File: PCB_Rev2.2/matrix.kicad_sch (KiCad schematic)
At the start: 9 parts, among them SW10 SW_Push, SW2 RotaryEncoder_Switch_MP, SW3 RotaryEncoder_Switch_MP, SW4 SW_Push, SW5 SW_Push, SW6 SW_Push, SW7 SW_Push, SW8 SW_Push, SW9 SW_Push

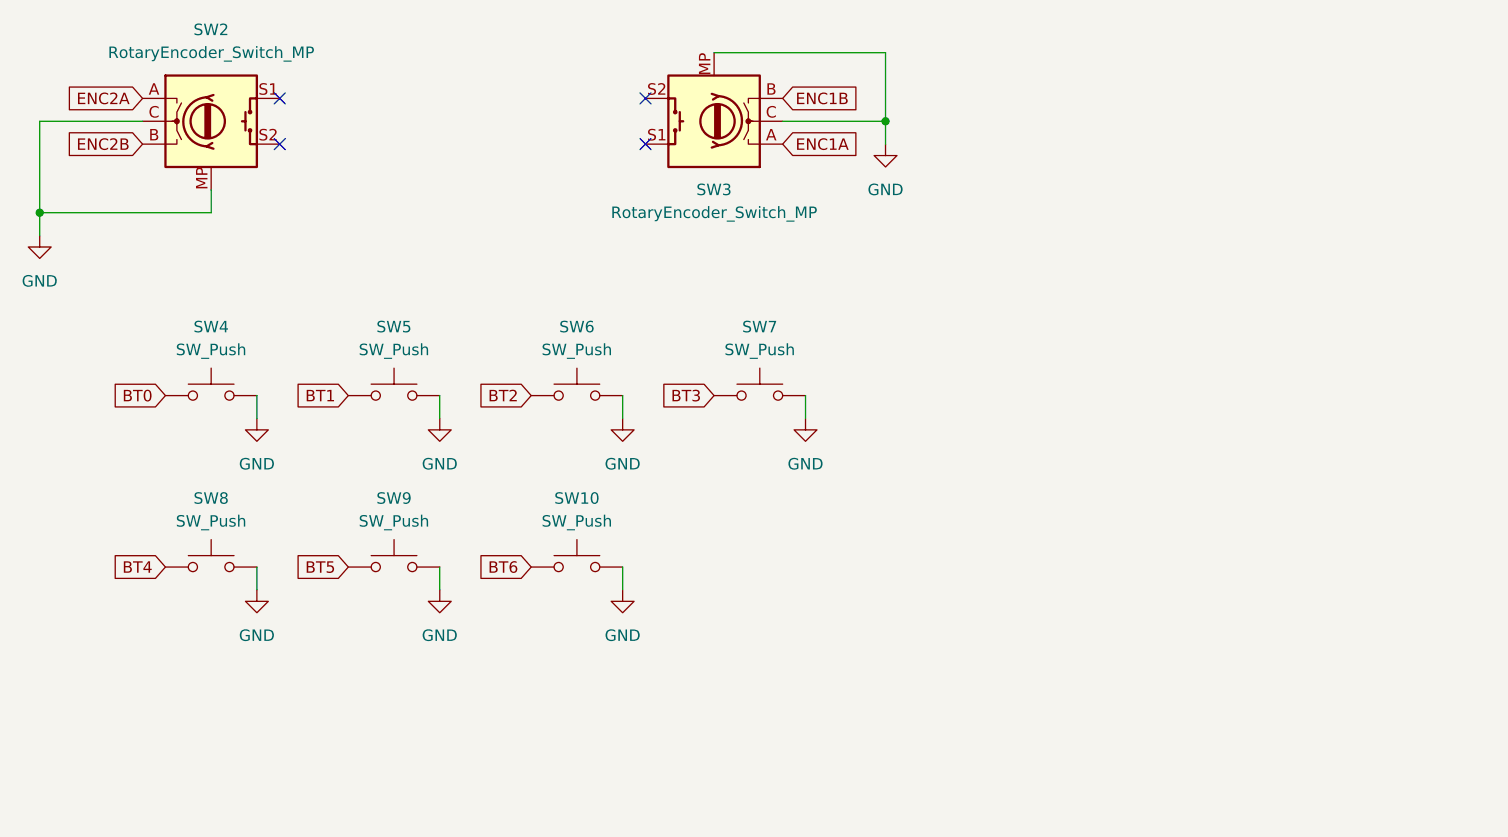
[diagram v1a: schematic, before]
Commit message: Before merge & open source.
Co-Authored-By: MAltmann <57740314+maltmannx@users.noreply.github.com>
Co-Authored-By: nonameCCC <79012391+nonameCCC@users.noreply.github.com>
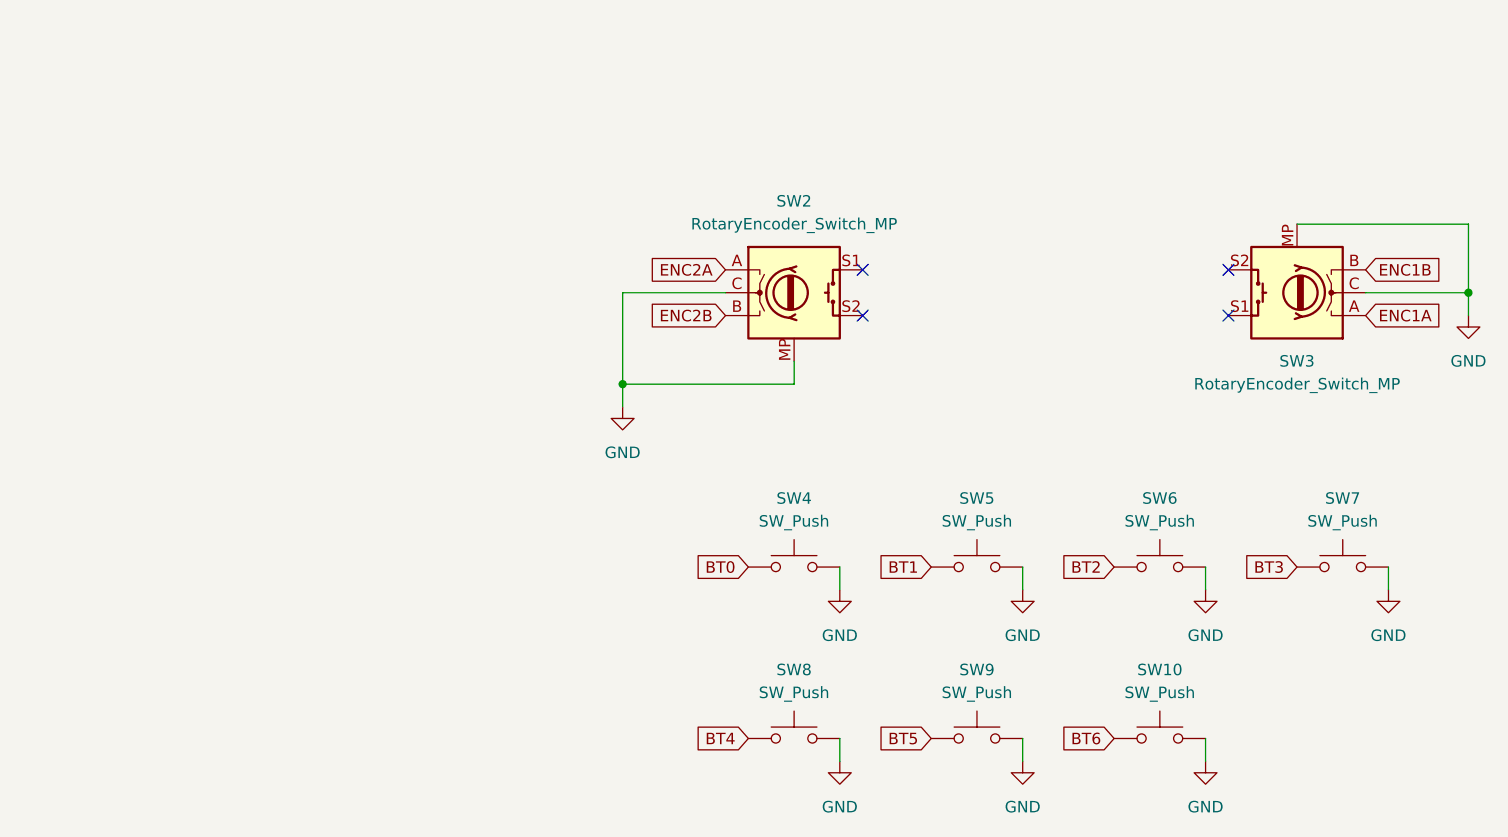
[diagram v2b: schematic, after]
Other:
- company: (none) -> Team PHDesign
- title: (none) -> PH-AC  --Arcade controller for Genshin-impact-like games.
- moved on the sheet: SW10, SW2, SW3, SW4, SW5, SW6, SW7, SW8, SW9
